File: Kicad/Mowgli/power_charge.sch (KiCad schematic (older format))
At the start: 18 parts, among them J2 Charge, J3 POWER, Q4 N06N-HIGH, Q4 N06N-LOW, SW1 Power Switch, U10 LM5109MA

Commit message: added PA3 ADC input pin
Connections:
- net labels added: Charge_Voltage
- wire segments 67 -> 68
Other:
- note added: "unknown ?"
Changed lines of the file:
@@
 Wire Wire Line
 	4050 1650 4050 1750
+Text HLabel 2850 1050 0    39   Output ~ 0
+Charge_Voltage
+Wire Wire Line
+	2850 1050 3100 1050
+Text Notes 3150 1050 0    39   ~ 0
+unknown ?
 $EndSCHEMATC

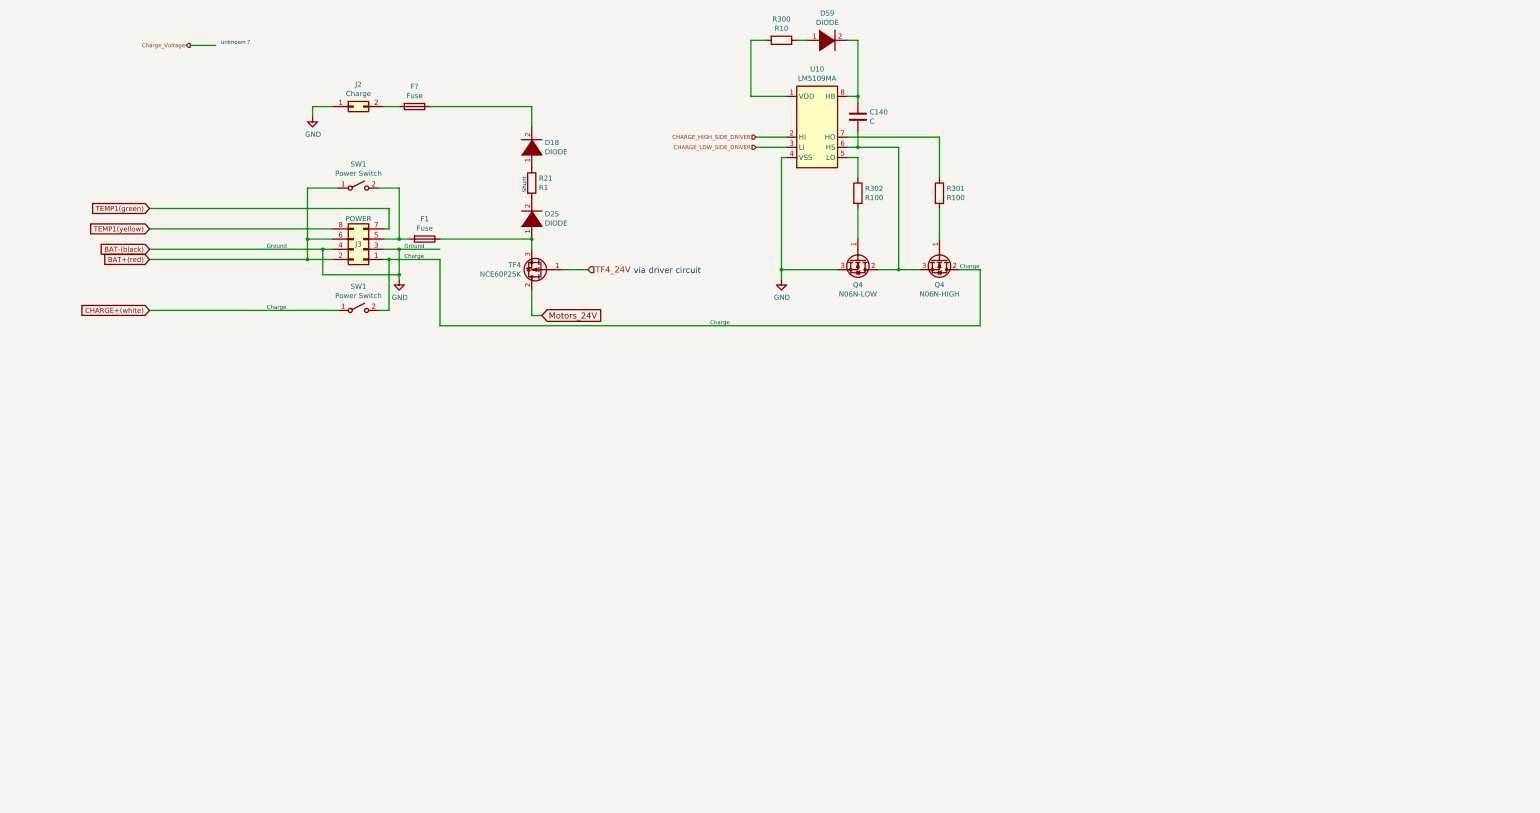
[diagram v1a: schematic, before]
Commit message: PA2,PA3 are used for Charging and Battery Voltage monitoring - added stm32 code and updated KiCad
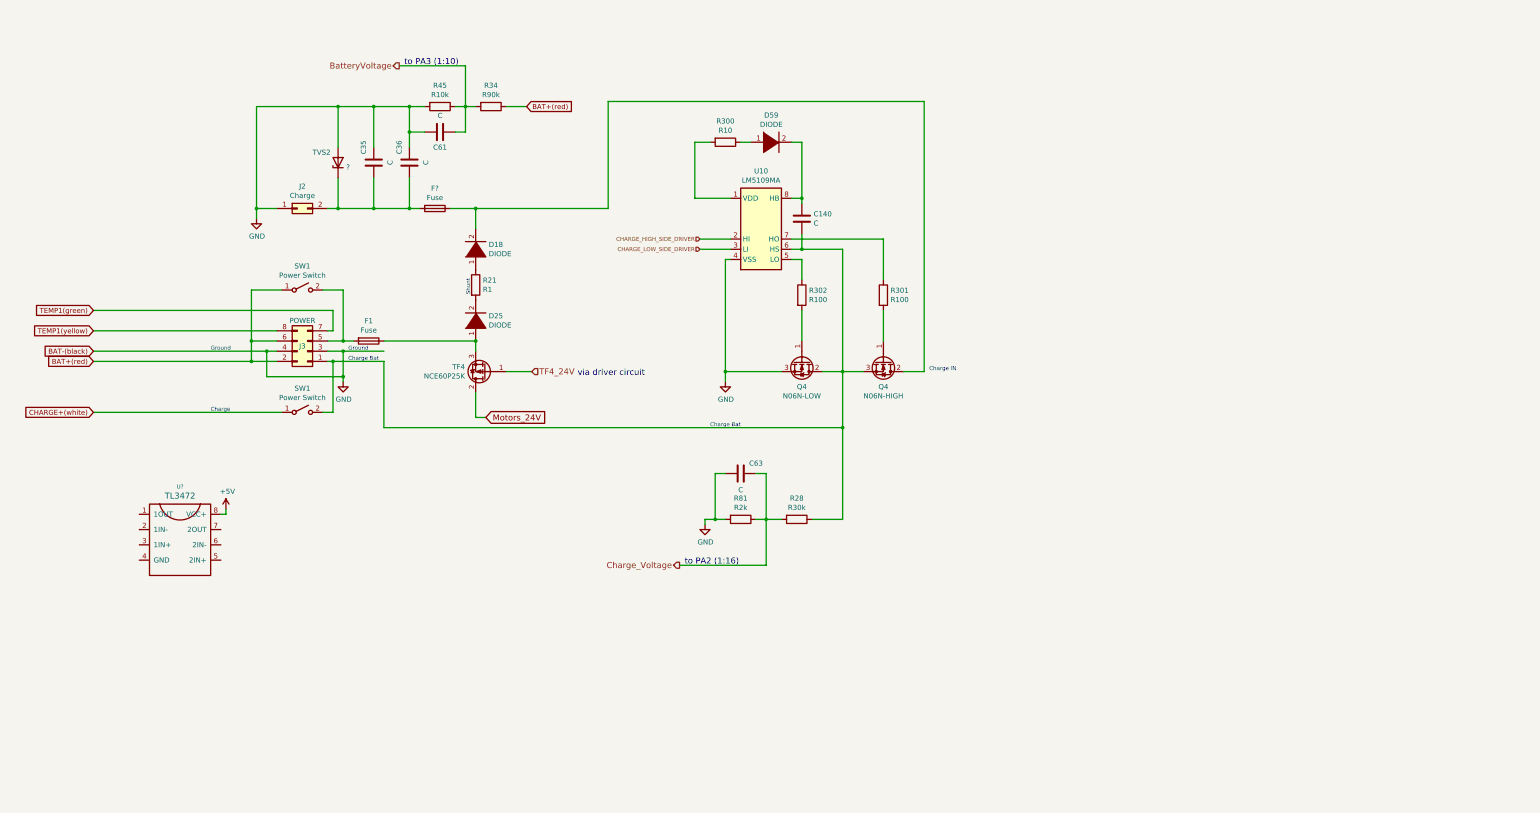
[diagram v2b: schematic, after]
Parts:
- added C35, C36, C61, C63: C, symbol Device:C
- added R28: R30k, symbol Device:R
- added R34: R90k, symbol Device:R
- added R45: R10k, symbol Device:R
- added R81: R2k, symbol Device:R
- added TVS2: ?, symbol Device:D_Zener
- added U?: TL3472, symbol Amplifier_Audio:TL3472
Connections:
- net labels added: +5V, BatteryVoltage
- wire segments 68 -> 109
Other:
- note added: "Charge Bat"
- note added: "Charge IN"
- note added: "to PA2 (1:16)"
- note added: "to PA3 (1:10)"
- note removed: "unknown ?"
- moved on the sheet: C140, D18, D25, D59, F1, F?, J2, J3, Q4, R21, R300, R301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

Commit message: updated kicad
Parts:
- added C103, C84: 220uF, symbol Device:C
- added C90: C, symbol Device:C
- added L2: L, symbol Device:L
- added R107, R32, R37: 1k, symbol Device:R
- added R22, R24, R33, R36: 12k, symbol Device:R
- added R278: 100k, symbol Device:R
- added R38: 0.1, symbol Device:R
- added TF1: YAS7/BSS83P, Package_TO_SOT_SMD:SOT-23, symbol Transistor_FET:AO3401A
- R28: value R30k -> 30k
- R300: value R10 -> 10
- R301, R302: value R100 -> 100
- R34: value R90k -> 90k
- R45: value R10k -> 10k
- R81: value R2k -> 2k
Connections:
- net +5V: now also R22.1
- net BAT+(red): no longer R34.1
- net GND: now also U?.4 (GND), C90.1, R24.2; no longer J3.3 (Pin_3), J3.4 (Pin_4)
- net at C140.2, J3.1 (Pin_1), Q4.2 (D)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: now also L2.2; no longer R28.1
- net at D18.2 (A), F?.1, Q4.2 (D): now also C103.2
- net at D25.1 (K), F1.1, TF4.3 (S): now also R278.2, TF1.2 (S)
- net at U?.1 (1OUT): now also U?.2 (1IN-), R33.1
- net at U?.3 (1IN+): now also R22.2, R24.1
- net at U?.5 (2IN+): now also R33.2, R37.1
- net at U?.6 (2IN-): now also R32.1, R36.1
- net at U?.7 (2OUT): now also R107.1, R36.2
- net TEMP1(green) renamed TEMP(green)
- net TEMP1(yellow) renamed OV(yellow)
- new net: R34.1, TF1.3 (D)
- new net: C84.1, L2.1, R28.1
- new net: C84.2, R37.2, R38.1
- new net: C103.1, R32.2, R38.2
- new net: R278.1, TF1.1 (G)
- new net BAT-(black): J3.3 (Pin_3), J3.4 (Pin_4)
- new net ChargeCurrent: C90.2, R107.2
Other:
- note added: "to PA1 (1:?)"
- moved on the sheet: C140, C35, C36, C61, C63, D18, D25, D59, F1, F?, J2, J3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

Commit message: kicad cleanup
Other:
- note added: "to PA1\n\ni=(Vout-2.5) x (100/12)"
- note removed: "to PA1 (1:?)"
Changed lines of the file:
@@
 $Descr A3 16535 11693
 encoding utf-8
-Sheet 10 14
+Sheet 8 14
 Title ""
 Date ""
@@
 Wire Wire Line
 	10450 8500 15150 8500
-Text Notes 15150 5000 0    59   ~ 0
-to PA1 (1:?)
+Text Notes 14650 4950 0    59   ~ 0
+to PA1\n\ni=(Vout-2.5) x (100/12)
 Wire Wire Line
 	5450 5000 6850 5000
